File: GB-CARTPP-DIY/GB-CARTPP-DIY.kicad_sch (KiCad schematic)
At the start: 31 parts

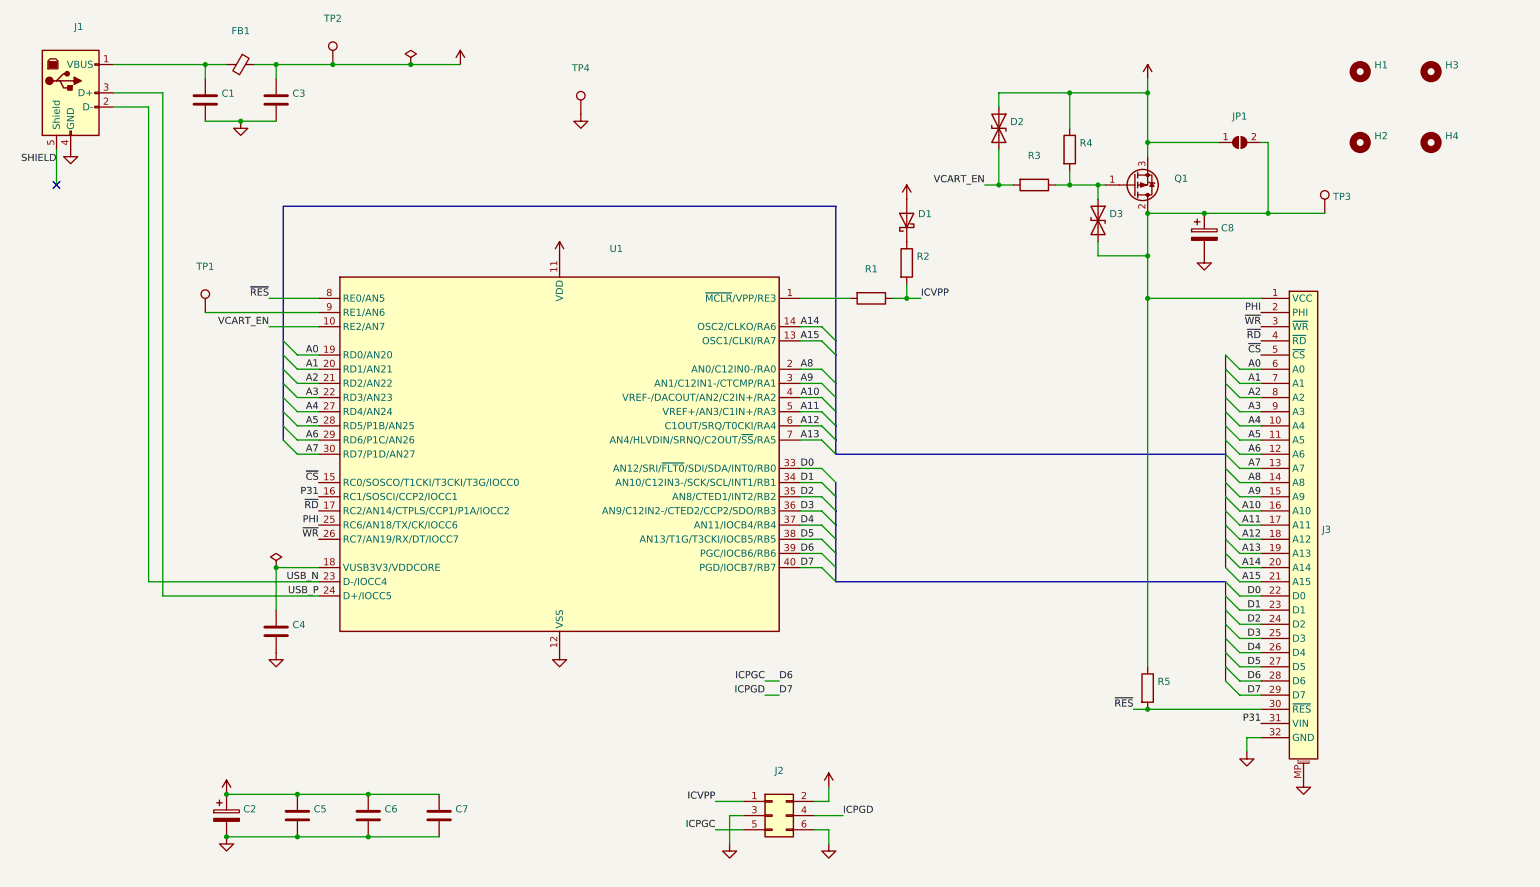
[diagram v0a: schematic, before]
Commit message: Upgrade projects to KiCad 7
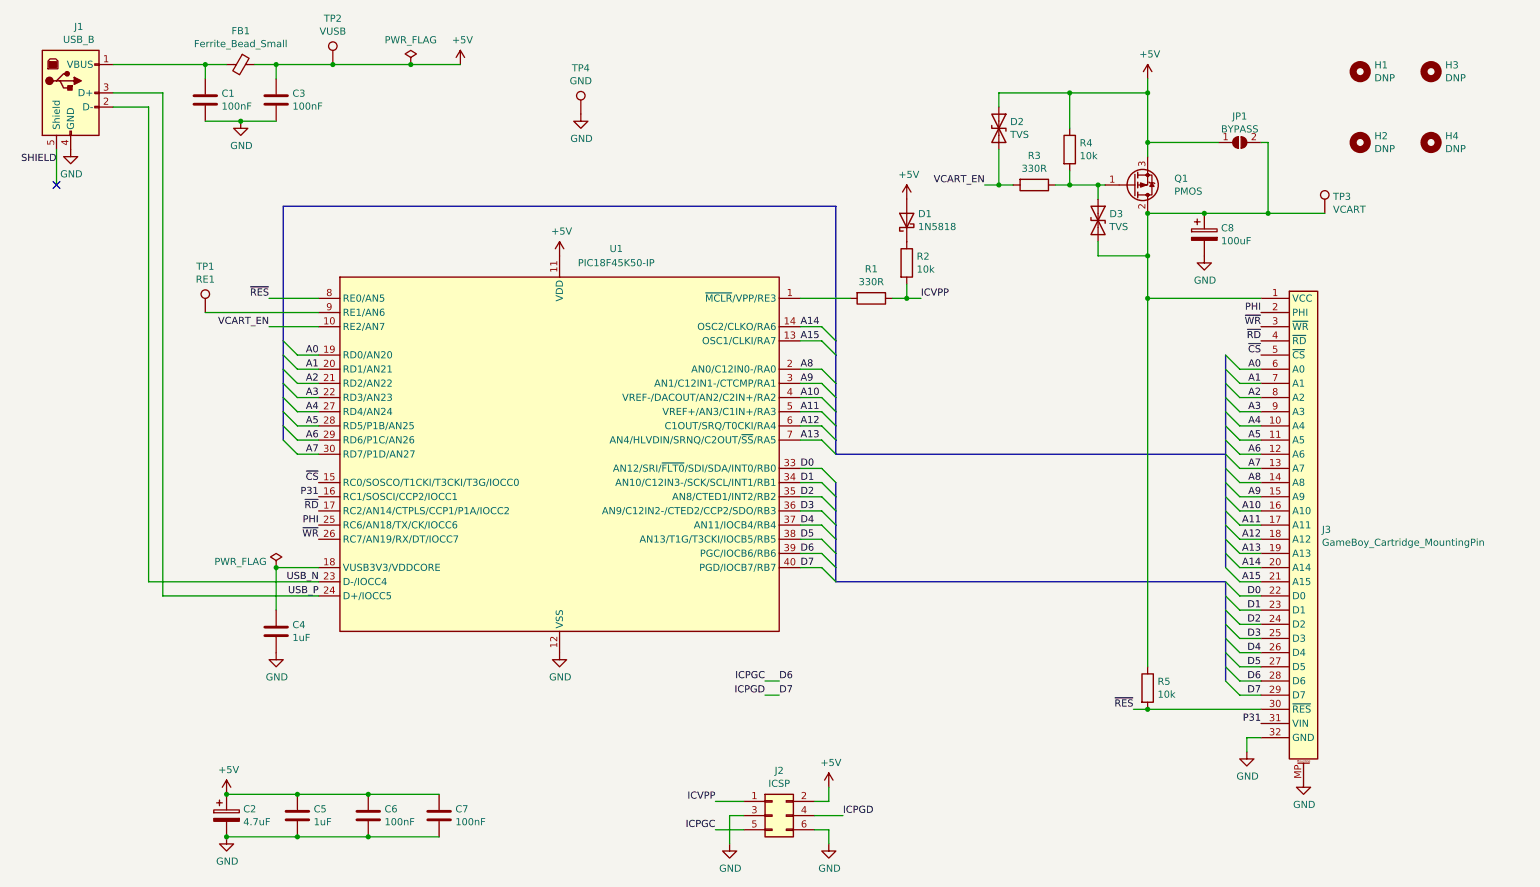
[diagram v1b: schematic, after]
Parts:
- C1, C3, C6, C7: value (none) -> 100nF; footprint (none) -> Capacitor_THT:C_Disc_D10.5mm_W5.0mm_P5.00mm
- C2: value (none) -> 4.7uF; footprint (none) -> Capacitor_THT:CP_Radial_D6.3mm_P2.50mm
- C4, C5: value (none) -> 1uF; footprint (none) -> Capacitor_THT:C_Disc_D10.5mm_W5.0mm_P5.00mm
- C8: value (none) -> 100uF; footprint (none) -> Capacitor_THT:CP_Radial_D6.3mm_P2.50mm
- D1: value (none) -> 1N5818; footprint (none) -> Diode_THT:D_DO-41_SOD81_P10.16mm_Horizontal
- D2, D3: value (none) -> TVS; footprint (none) -> Diode_THT:D_DO-41_SOD81_P10.16mm_Horizontal
- FB1: value (none) -> Ferrite_Bead_Small; footprint (none) -> Resistor_THT:R_Axial_DIN0411_L9.9mm_D3.6mm_P20.32mm_Horizontal
- H1, H2, H3, H4: value (none) -> DNP; footprint (none) -> MountingHole:MountingHole_5.3mm_M5
- J1: value (none) -> USB_B; footprint (none) -> Connector_USB:USB_B_Lumberg_2411_02_Horizontal
- J2: value (none) -> ICSP; footprint (none) -> Connector_PinHeader_2.54mm:PinHeader_2x03_P2.54mm_Vertical
- J3: value (none) -> GameBoy_Cartridge_MountingPin; footprint (none) -> Gekkio_Connector_PCBEdge:GameBoy_Cartridge_AGS_1x32-1MP_P1.50mm_Socket_Horizontal
- JP1: value (none) -> BYPASS; footprint (none) -> Jumper:SolderJumper-2_P1.3mm_Open_RoundedPad1.0x1.5mm
- Q1: value (none) -> PMOS; footprint (none) -> Package_TO_SOT_THT:TO-220-3_Vertical
- R1, R3: value (none) -> 330R; footprint (none) -> Resistor_THT:R_Axial_DIN0207_L6.3mm_D2.5mm_P7.62mm_Horizontal
- R2, R4, R5: value (none) -> 10k; footprint (none) -> Resistor_THT:R_Axial_DIN0207_L6.3mm_D2.5mm_P7.62mm_Horizontal
- TP1: value (none) -> RE1; footprint (none) -> TestPoint:TestPoint_THTPad_D2.0mm_Drill1.0mm
- TP2: value (none) -> VUSB; footprint (none) -> TestPoint:TestPoint_THTPad_D2.0mm_Drill1.0mm
- TP3: value (none) -> VCART; footprint (none) -> TestPoint:TestPoint_THTPad_D2.0mm_Drill1.0mm
- TP4: value (none) -> GND; footprint (none) -> TestPoint:TestPoint_THTPad_D2.0mm_Drill1.0mm
- U1: value (none) -> PIC18F45K50-IP; footprint (none) -> Package_DIP:DIP-40_W15.24mm_Socket_LongPads
